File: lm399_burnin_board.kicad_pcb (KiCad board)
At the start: 4 copper layers, 160 x 100 mm, 287 parts, among them J1 C64AC, J2 DB50_Female, U1 OPA4202, U10 LM399, U11 OPA4202, U12 LM399, U13 LM399, U14 LM399, U15 LM399, U16 OPA4202, U17 LM399, U18 LM399, U19 LM399, U2 LM399, U20 LM399, U21 OPA4202, U22 LM399, U23 LM399, U24 LM399, U25 LM399, U26 LT1085-ADJ, U3 LM399, U4 LM399, U5 LM399, U6 OPA4202, U7 LM399, U8 LM399, U9 LM399

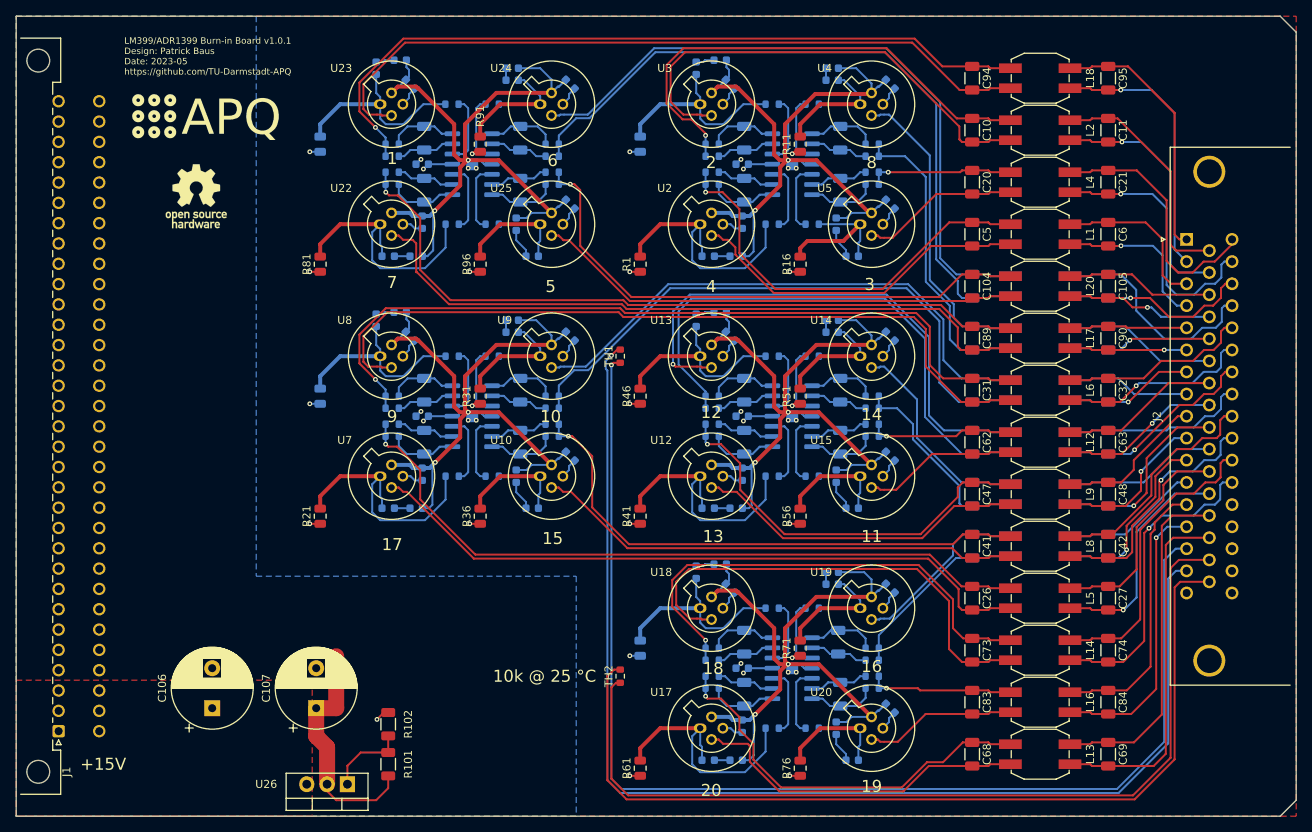
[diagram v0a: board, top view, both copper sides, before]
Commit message: Updated references to follow geographical rules
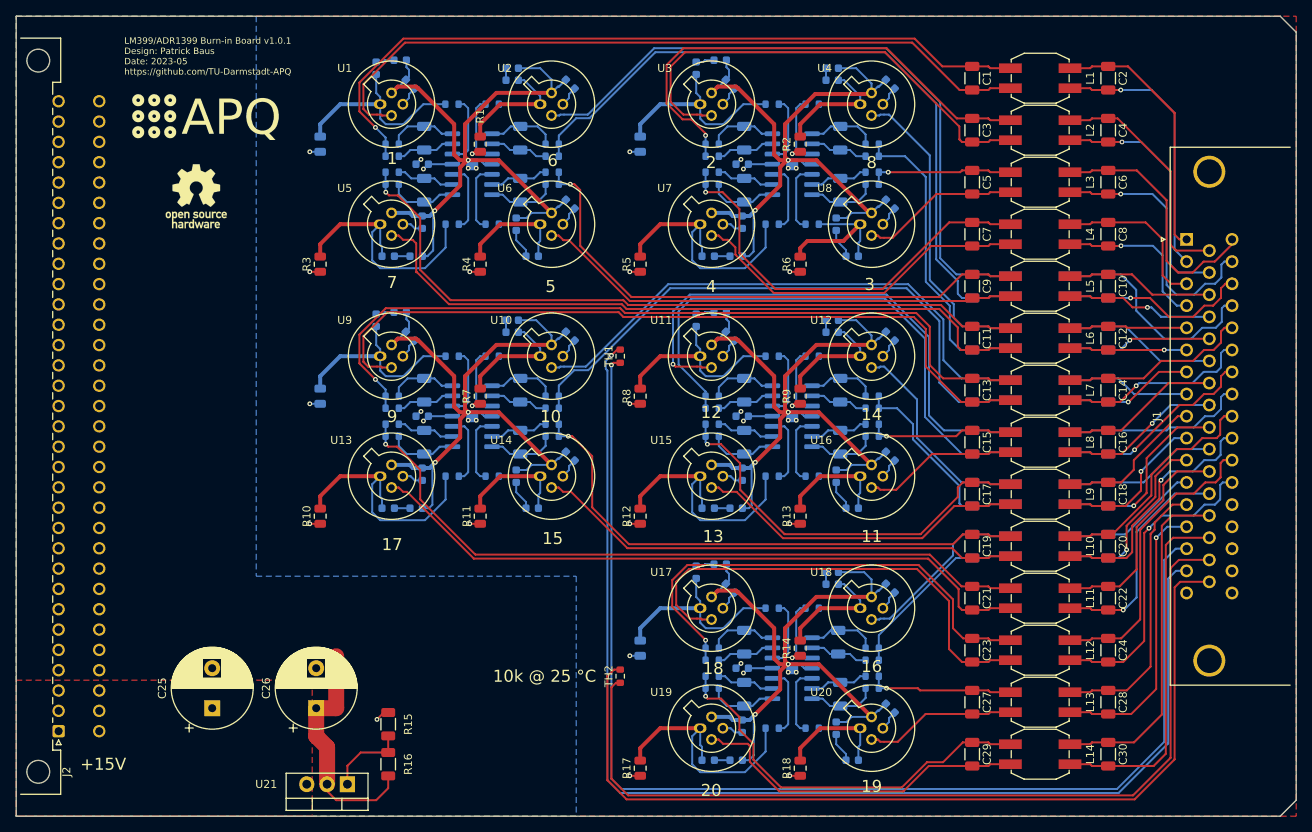
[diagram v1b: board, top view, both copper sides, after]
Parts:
- renumbered C94 to C1, C105 to C10, C72 to C100, C82 to C101, C67 to C102, C64 to C103, C70 to C104, C81 to C105, C75 to C106, C66 to C107, C89 to C11, C90 to C12, C31 to C13, C32 to C14, C62 to C15, C63 to C16, C47 to C17, C48 to C18, C41 to C19, C95 to C2, C42 to C20, C26 to C21, C27 to C22, C73 to C23, C74 to C24, C106 to C25, C107 to C26, C83 to C27, C84 to C28, C68 to C29, C10 to C3, C69 to C30, C12 to C31, C13 to C32, C7 to C33, C8 to C34, C86 to C35, C97 to C36, C101 to C37, C92 to C38, C14 to C39, C11 to C4, C9 to C40, C1 to C41, C98 to C42, C85 to C43, C93 to C44, C17 to C45, C19 to C46, C4 to C47, C91 to C48, C103 to C49, C20 to C5, C88 to C50, C18 to C51, C2 to C52, C102 to C53, C96 to C54, C100 to C55, C99 to C56, C3 to C57, C87 to C58, C55 to C59, C21 to C6, C50 to C60, C34 to C61, C29 to C62, C16 to C63, C15 to C64, C44 to C65, C59 to C66, C23 to C67, C38 to C68, C37 to C69, C5 to C7, C36 to C70, C56 to C71, C51 to C72, C35 to C73, C30 to C74, C53 to C75, C52 to C76, C61 to C77, C43 to C78, C46 to C79, C6 to C8, C40 to C80, C25 to C81, C22 to C82, C49 to C83, C60 to C84, C54 to C85, C28 to C86, C39 to C87, C33 to C88, C58 to C89, C104 to C9, C57 to C90, C45 to C91, C24 to C92, C79 to C93, C78 to C94, C76 to C95, C71 to C96, C65 to C97, C80 to C98, C77 to C99, J2 to J1, J1 to J2, L18 to L1, L8 to L10, L5 to L11, L14 to L12, L16 to L13, L13 to L14, L19 to L15, L3 to L16, L7 to L17, L10 to L18, L11 to L19, L15 to L20, L4 to L3, L1 to L4, L20 to L5, L17 to L6, L6 to L7, L12 to L8, NT10 to NT1, NT16 to NT10, NT1 to NT11, NT4 to NT12, NT6 to NT13, NT46 to NT14, NT5 to NT15, NT8 to NT16, NT19 to NT17, NT11 to NT18, NT25 to NT19, NT18 to NT2, NT23 to NT20, NT3 to NT21, NT15 to NT22, NT21 to NT23, NT7 to NT25, NT22 to NT26, NT9 to NT3, NT12 to NT4, NT17 to NT5, NT20 to NT6, NT14 to NT7, NT2 to NT8, NT13 to NT9, R91 to R1, R21 to R10, R63 to R100, R77 to R101, R62 to R102, R36 to R11, R41 to R12, R56 to R13, R71 to R14, R102 to R15, R101 to R16, R61 to R17, R76 to R18, R12 to R19, R11 to R2, R7 to R20, R92 to R21, R87 to R22, R13 to R23, R8 to R24, R93 to R25, R88 to R26, R14 to R27, R15 to R28, R9 to R29, R81 to R3, R10 to R30, R6 to R31, R95 to R32, R94 to R33, R90 to R34, R89 to R35, R86 to R36, R19 to R37, R20 to R38, R4 to R39, R96 to R4, R5 to R40, R99 to R41, R100 to R42, R84 to R43, R85 to R44, R18 to R45, R3 to R46, R98 to R47, R83 to R48, R17 to R49, R1 to R5, R2 to R50, R97 to R51, R82 to R52, R47 to R53, R27 to R54, R52 to R55, R53 to R56, R48 to R57, R33 to R58, R32 to R59, R16 to R6, R28 to R60, R55 to R61, R54 to R62, R50 to R63, R49 to R64, R35 to R65, R34 to R66, R29 to R67, R30 to R68, R26 to R69, R31 to R7, R59 to R70, R60 to R71, R45 to R72, R44 to R73, R39 to R74, R40 to R75, R25 to R76, R24 to R77, R58 to R78, R43 to R79, R46 to R8, R38 to R80, R23 to R81, R57 to R82, R42 to R83, R37 to R84, R22 to R85, R67 to R86, R72 to R87, R73 to R88, R68 to R89, R51 to R9, R74 to R90, R69 to R91, R66 to R92, R75 to R93, R79 to R94, R80 to R95, R65 to R96, R70 to R97, R64 to R98, R78 to R99, U23 to U1, U9 to U10, U13 to U11, U14 to U12, U7 to U13, U10 to U14, U12 to U15, U15 to U16, U18 to U17, U19 to U18, U17 to U19, U24 to U2, U26 to U21, U1 to U22, U21 to U23, U11 to U24, U6 to U25, U16 to U26, U22 to U5, U25 to U6, U2 to U7, U5 to U8, U8 to U9
